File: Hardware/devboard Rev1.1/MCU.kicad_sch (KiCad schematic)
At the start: 8 parts, among them SW2 EN, SW3 BOOT, U3 ESP32-WROOM-32E-R2

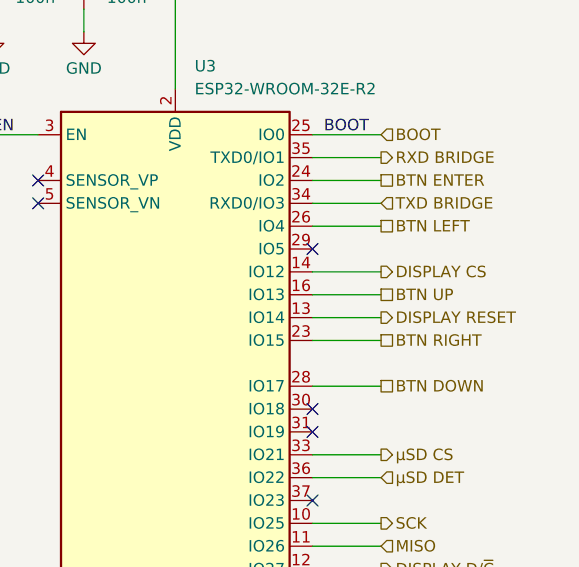
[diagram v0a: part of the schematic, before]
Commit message: fixed switch footprint and changed buttons pins to avoid bootstrapping pins
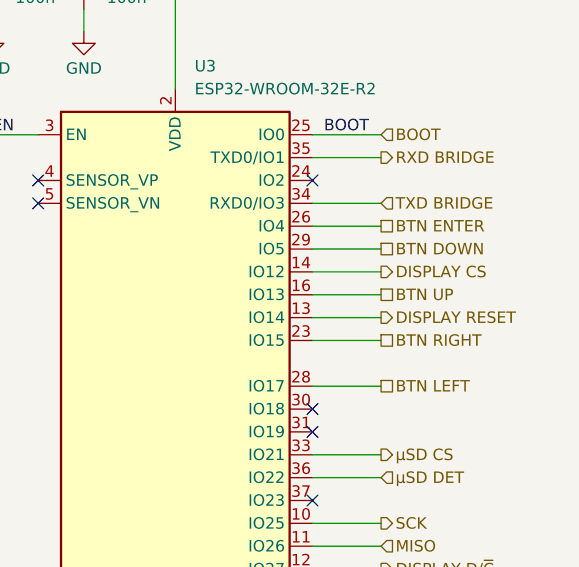
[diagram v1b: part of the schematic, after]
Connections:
- net BTN DOWN: now also U3.29 (IO5); no longer U3.28 (IO17)
- net BTN ENTER: now also U3.26 (IO4); no longer U3.24 (IO2)
- net BTN LEFT: now also U3.28 (IO17); no longer U3.26 (IO4)
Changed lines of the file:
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@@
 	)
 	(no_connect
-		(at 165.1 82.55)
+		(at 165.1 74.93)
 	)
 	(no_connect
@@
 	(wire
 		(pts
-			(xy 172.72 74.93) (xy 165.1 74.93)
-		)
-		(stroke
-			(width 0)
-			(type default)
-		)
-	)
-	(wire
-		(pts
 			(xy 165.1 87.63) (xy 172.72 87.63)
 		)
@@
 		(pts
 			(xy 81.28 109.22) (xy 90.17 109.22)
+		)
+		(stroke
+			(width 0)
+			(type default)
+		)
+	)
+	(wire
+		(pts
+			(xy 172.72 82.55) (xy 165.1 82.55)
 		)
 		(stroke
@@
 		(shape output)
 		(at 172.72 105.41 0)
-		(effects
-			(font
-				(size 1.27 1.27)
-			)
-			(justify left)
-		)
-	)
-	(hierarchical_label "BTN ENTER"
-		(shape passive)
-		(at 172.72 74.93 0)
 		(effects
 			(font
@@
 	(hierarchical_label "BTN DOWN"
 		(shape passive)
-		(at 172.72 97.79 0)
+		(at 172.72 82.55 0)
+		(effects
+			(font
+				(size 1.27 1.27)
+			)
+			(justify left)
+		)
+	)
+	(hierarchical_label "BTN ENTER"
+		(shape passive)
+		(at 172.72 80.01 0)
 		(effects
 			(font
@@
 	(hierarchical_label "BTN LEFT"
 		(shape passive)
-		(at 172.72 80.01 0)
-		(effects
-			(font
+		(at 172.72 97.79 0)
+		(effects
+			(font
